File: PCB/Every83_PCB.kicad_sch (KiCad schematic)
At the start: 42 parts, among them J1 781710004, J2 Conn_01x08_Socket, J3 Conn_01x02_Socket, J4 Conn_01x03_Pin, J5 Conn_01x08_Socket, J6 Conn_01x02_Pin, J7 Conn_02x03_Counter_Clockwise, Q1 MMDT2222A, Q2 2N7002, Q3 DMG2305, Q4 AO3401A, SW101 KMR2, SW102 KMR2, U1 Core52840, U2 AP2112(3.3V), U3 MCP73831T-2ACI/OT

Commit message: Removing neopixels WIP
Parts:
- removed R16: 470R, Resistor_SMD:R_0603_1608Metric, symbol Device:R
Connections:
- net 3.3V: no longer Q4.3 (D), R15.2
- net V_Raw: now reaches C7.2, D101.1 (C), Q3.2 (S), R8.2, U2.1 (IN)
- net V_Raw: now also Q4.3 (D), R15.2
- no-connect marks 1 -> 2
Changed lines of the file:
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@@
 	)
 	(no_connect
+		(at 167.64 109.22)
+	)
+	(no_connect
 		(at 180.34 245.11)
 	)
@@
 		)
 	)
+	(global_label "V_Raw"
+		(shape input)
+		(at 149.86 240.03 90)
+		(fields_autoplaced yes)
+		(effects
+			(font
+				(size 1.27 1.27)
+			)
+			(justify left)
+		)
+		(property "Intersheetrefs" "${INTERSHEET_REFS}"
+			(at 149.86 231.2391 90)
+			(effects
+				(font
+					(size 1.27 1.27)
+				)
+				(justify left)
+				(hide yes)
+			)
+		)
+	)
 	(global_label "16"
 		(shape input)
@@
 		)
 	)
-	(global_label "NEOPIX"
+	(global_label "V_Raw"
 		(shape input)
-		(at 175.26 109.22 0)
+		(at 251.46 168.91 90)
 		(fields_autoplaced yes)
 		(effects
@@
 		)
 		(property "Intersheetrefs" "${INTERSHEET_REFS}"
-			(at 185.1395 109.22 0)
+			(at 251.46 160.1191 90)
 			(effects
 				(font
@@
 	)
 	(symbol
-		(lib_id "Device:R")
-		(at 171.45 109.22 270)
-		(unit 1)
-		(exclude_from_sim no)
-		(in_bom yes)
-		(on_board yes)
-		(dnp no)
-		(fields_autoplaced yes)
-		(property "Reference" "R16"
-			(at 171.45 102.87 90)
-			(effects
-				(font
-					(size 1.27 1.27)
-				)
-			)
-		)
-		(property "Value" "470R"
-			(at 171.45 105.41 90)
-			(effects
-				(font
-					(size 1.27 1.27)
-				)
-			)
-		)
-		(property "Footprint" "Resistor_SMD:R_0603_1608Metric"
-			(at 171.45 107.442 90)
-			(effects
-				(font
-					(size 1.27 1.27)
-				)
-				(hide yes)
-			)
-		)
-		(property "Datasheet" "~"
-			(at 171.45 109.22 0)
-			(effects
-				(font
-					(size 1.27 1.27)
-				)
-				(hide yes)
-			)
-		)
-		(property "Description" "Resistor"
-			(at 171.45 109.22 0)
-			(effects
-				(font
-					(size 1.27 1.27)
-				)
-				(hide yes)
-			)
-		)
-		(pin "1"
-		)
-		(pin "2"
-		)
-		(instances
-			(project "Every83_PCB"
-				(path "/ea2432c4-eb7a-431a-b465-8c00cfcb4450"
-					(reference "R16")
-					(unit 1)
-				)
-			)
-		)
-	)
-	(symbol
 		(lib_id "Adafruit nRF52840 Bluefruit Feather Express Rev D-eagle-import:SWITCH_TACT_SMT4.6X2.8")
 		(at 66.04 187.96 0)
@@
 					(unit 1)
 				)
-			)
-		)
-	)
-	(symbol
-		(lib_id "Adafruit nRF52840 Bluefruit Feather Express Rev D-eagle-import:3.3V")
-		(at 251.46 166.37 0)
-		(unit 1)
-		(exclude_from_sim no)
-		(in_bom yes)
-		(on_board yes)
-		(dnp no)
-		(property "Reference" "#U$039"
-			(at 251.46 166.37 0)
-			(effects
-				(font
-					(size 1.27 1.27)
-				)
-				(hide yes)
-			)
-		)
-		(property "Value" "3.3V"
-			(at 249.936 165.354 0)
-			(effects
-				(font
-					(size 1.27 1.0795)
-				)
-				(justify left bottom)
-			)
-		)
-		(property "Footprint" ""
-			(at 251.46 166.37 0)
-			(effects
-				(font
-					(size 1.27 1.27)
-				)
-				(hide yes)
-			)
-		)
-		(property "Datasheet" ""
-			(at 251.46 166.37 0)
-			(effects
-				(font
-					(size 1.27 1.27)
-				)
-				(hide yes)
-			)
-		)
-		(property "Description" ""
-			(at 251.46 166.37 0)
-			(effects
-				(font
-					(size 1.27 1.27)
-				)
-				(hide yes)
-			)
-		)
-		(pin "1"
-		)
-		(instances
-			(project "Every83_PCB"
-				(path "/ea2432c4-eb7a-431a-b465-8c00cfcb4450"
-					(reference "#U$039")
-					(unit 1)
-				)

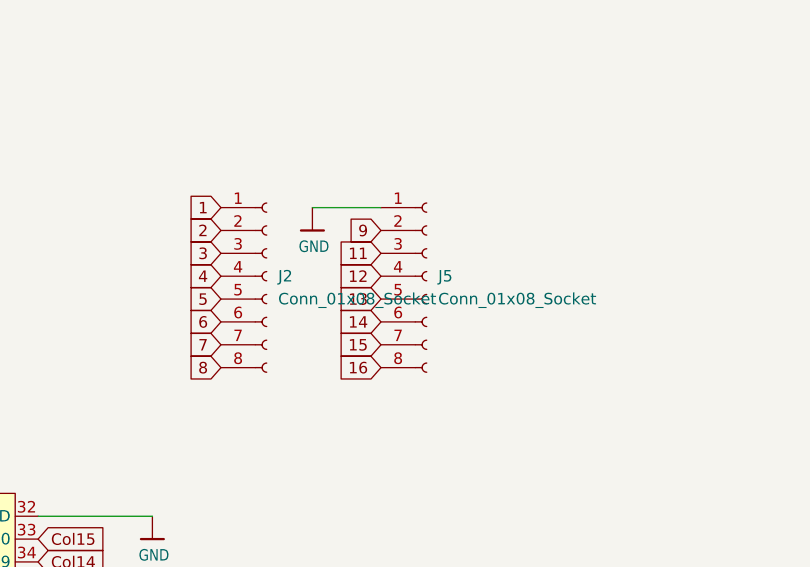
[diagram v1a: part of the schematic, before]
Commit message: removed pin headers
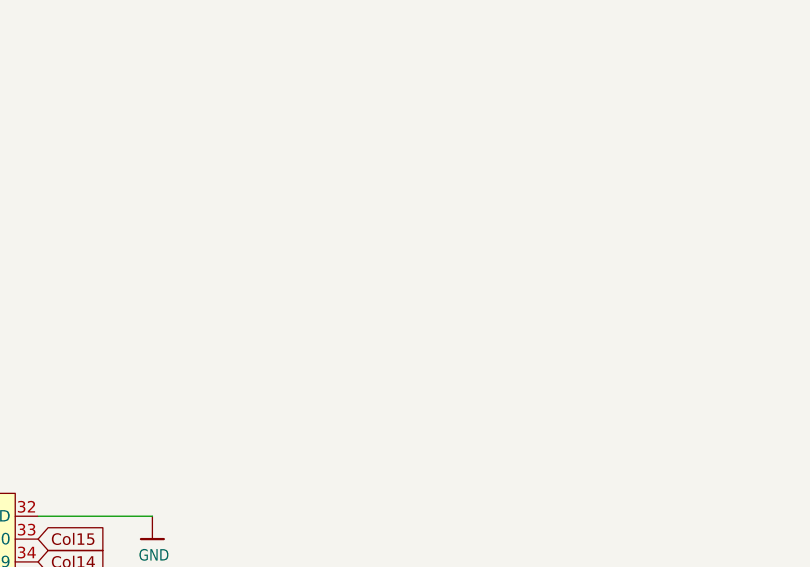
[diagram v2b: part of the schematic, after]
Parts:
- removed J2, J5: Conn_01x08_Socket, Connector_PinHeader_1.27mm:PinHeader_1x08_P1.27mm_Vertical, symbol Connector:Conn_01x08_Socket

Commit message: WIP
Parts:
- C3, C4: footprint Adafruit nRF52840 Bluefruit Feather Express Rev D:0603-NO -> Capacitor_SMD:C_0402_1005Metric
- C5, C7, C8: footprint Adafruit nRF52840 Bluefruit Feather Express Rev D:0805-NO -> Capacitor_SMD:C_0603_1608Metric
- C6, C9: value 10uF -> 4.7uF; footprint Adafruit nRF52840 Bluefruit Feather Express Rev D:0805-NO -> Capacitor_SMD:C_0603_1608Metric
- R1, R10, R13, R14, R15, R6, R7, R8, R9: footprint Resistor_SMD:R_0603_1608Metric -> Resistor_SMD:R_0402_1005Metric
- R4: footprint Adafruit nRF52840 Bluefruit Feather Express Rev D:0603-NO -> Resistor_SMD:R_0402_1005Metric
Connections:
- net GND: now also R4.1; no longer R4.2
- net at U3.5 (PROG): now also R4.2; no longer R4.1
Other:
- moved on the sheet: C6, R4

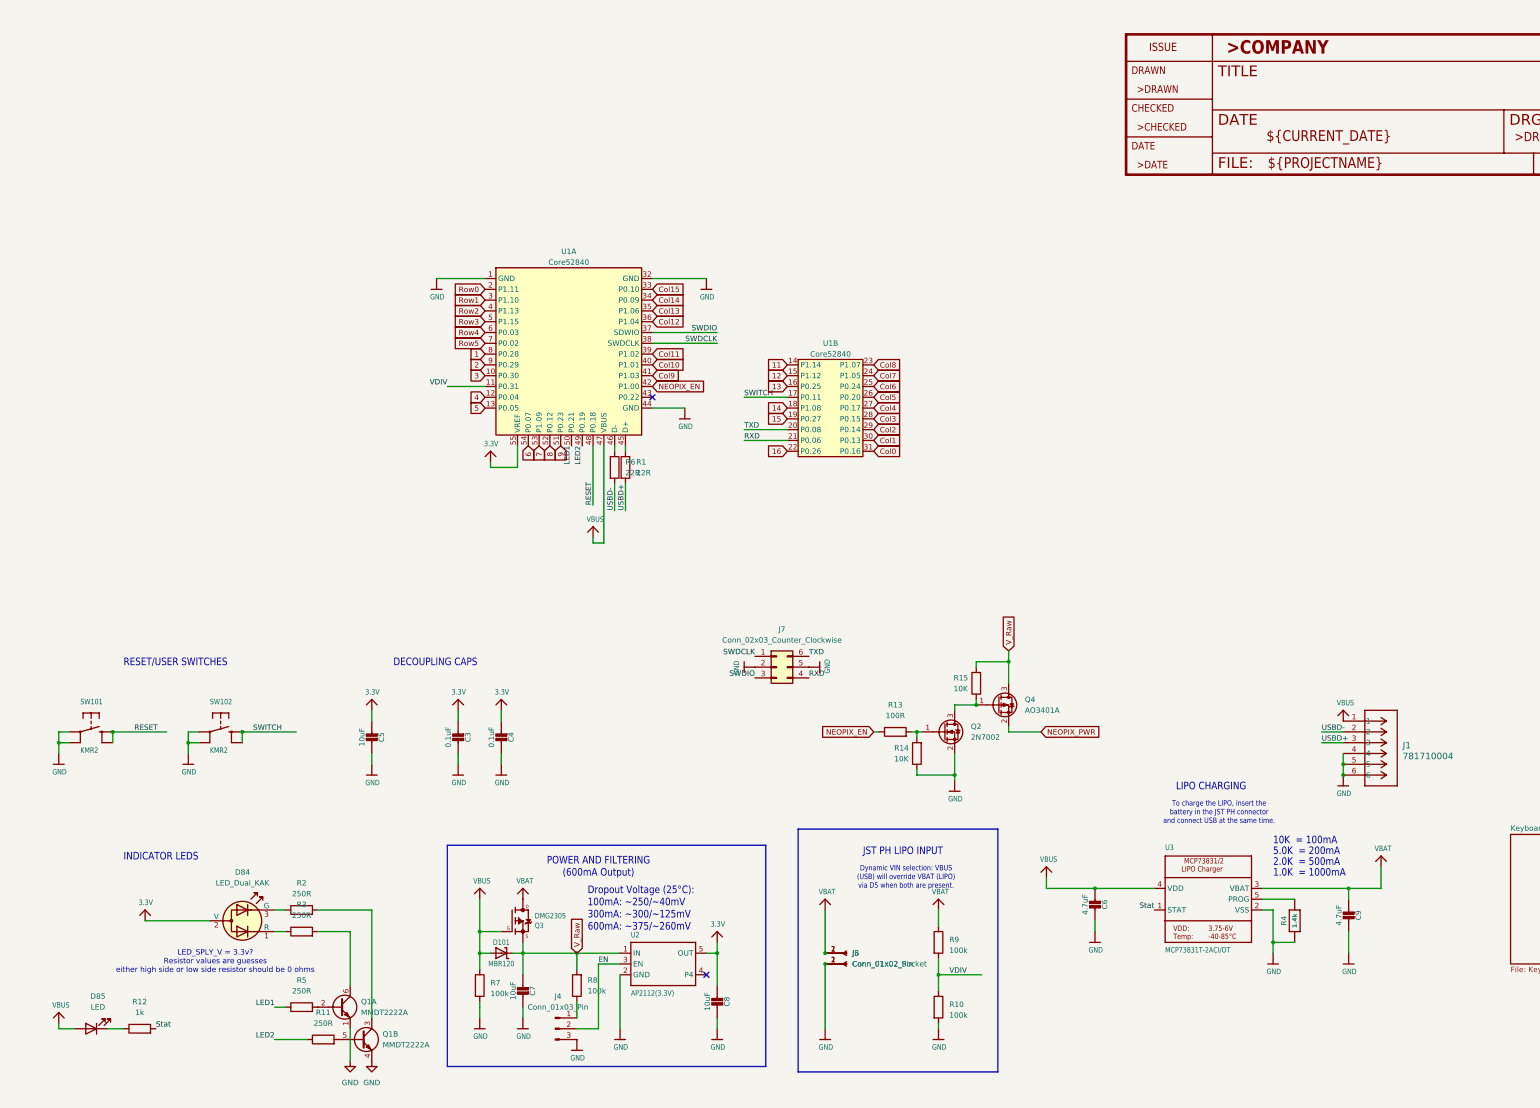
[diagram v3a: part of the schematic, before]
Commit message: Changed battery managment IC and LDO
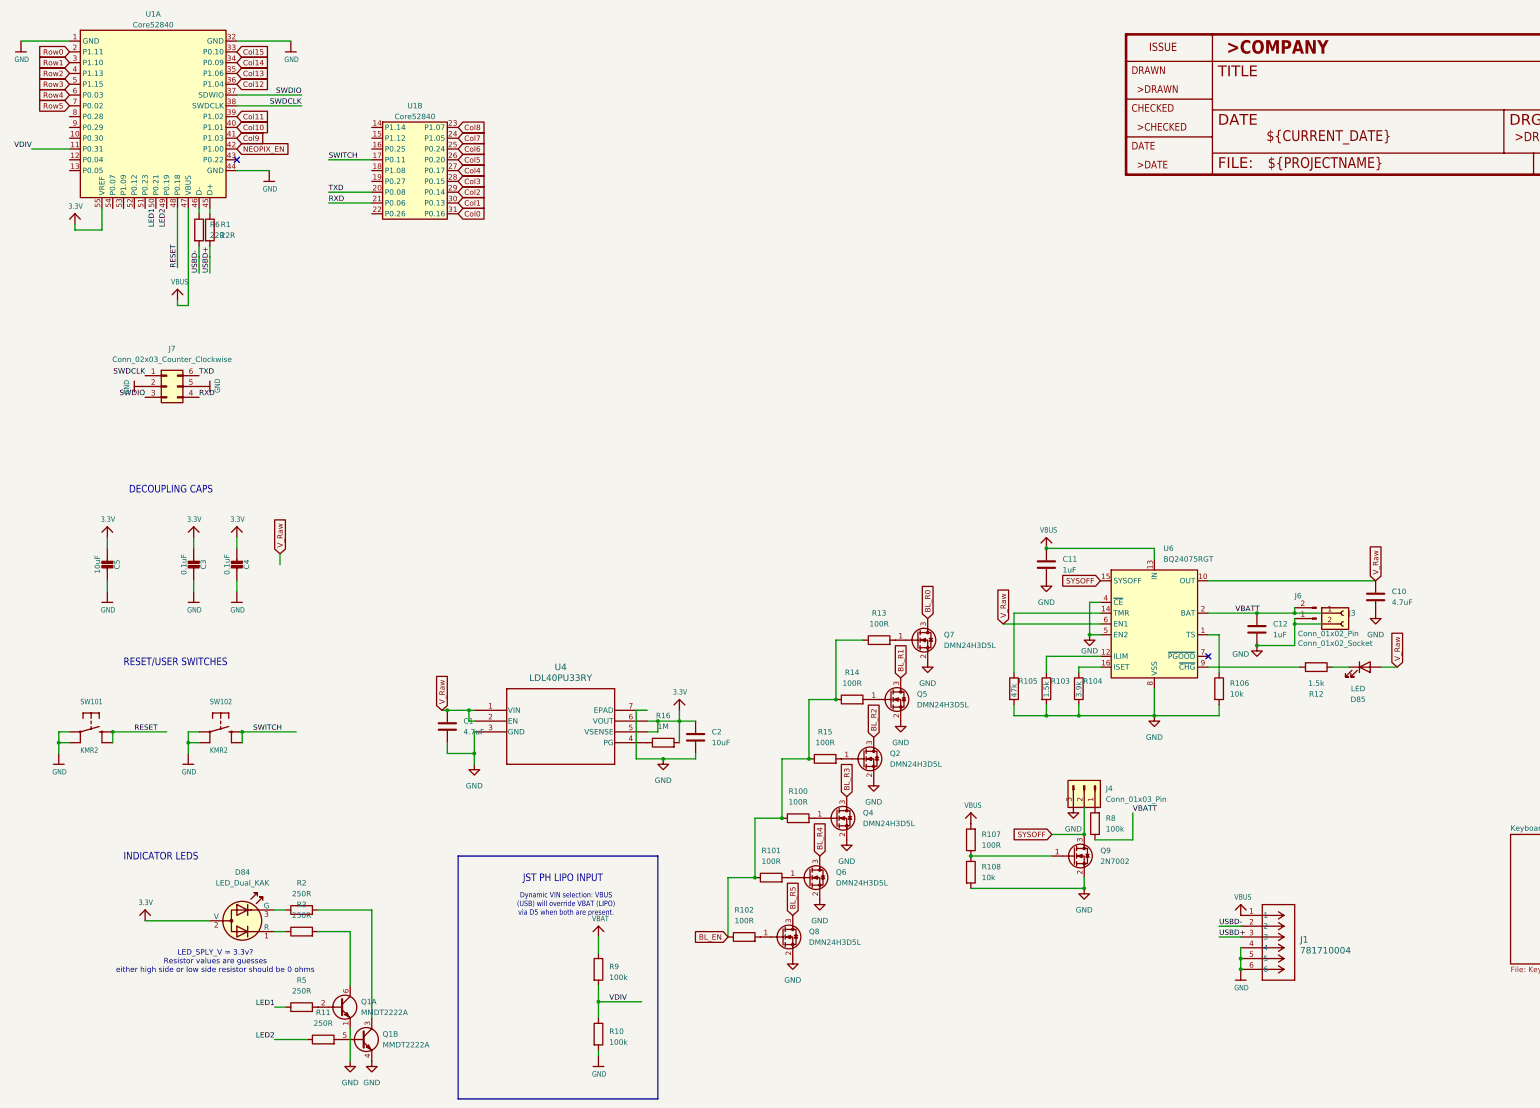
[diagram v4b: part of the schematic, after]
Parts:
- removed C6, C9: 4.7uF, Capacitor_SMD:C_0603_1608Metric, symbol Adafruit nRF52840 Bluefruit Feather Express Rev D-eagle-import:CAP_CERAMIC0805-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
- removed C7, C8: 10uF, Capacitor_SMD:C_0603_1608Metric, symbol Adafruit nRF52840 Bluefruit Feather Express Rev D-eagle-import:CAP_CERAMIC0805-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
- removed D101: MBR120, Diode_SMD:D_SOD-123, symbol Adafruit nRF52840 Bluefruit Feather Express Rev D-eagle-import:DIODE-SCHOTTKYSO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
- removed Q2: 2N7002, Package_TO_SOT_SMD:SOT-23, symbol Transistor_FET:2N7002
- removed Q3: DMG2305, Adafruit nRF52840 Bluefruit Feather Express Rev D:SOT23-R, symbol Adafruit nRF52840 Bluefruit Feather Express Rev D-eagle-import:MOSFET-P
- removed Q4: AO3401A, Package_TO_SOT_SMD:SOT-23, symbol Transistor_FET:AO3401A
- removed R4: 1.4k, Resistor_SMD:R_0402_1005Metric, symbol Adafruit nRF52840 Bluefruit Feather Express Rev D-eagle-import:RESISTOR_0603_NO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
- removed R7: 100k, Resistor_SMD:R_0402_1005Metric, symbol Device:R
- removed U2: AP2112(3.3V), Adafruit nRF52840 Bluefruit Feather Express Rev D:SOT23-5, symbol Adafruit nRF52840 Bluefruit Feather Express Rev D-eagle-import:VREG_SOT23-5
- removed U3: MCP73831T-2ACI/OT, Adafruit nRF52840 Bluefruit Feather Express Rev D:SOT23-5, symbol Adafruit nRF52840 Bluefruit Feather Express Rev D-eagle-import:MCP73831/2
- added C1, C10: 4.7uF, Capacitor_SMD:C_0402_1005Metric, symbol Device:C
- added C11, C12: 1uF, Capacitor_SMD:C_0402_1005Metric, symbol Device:C
- added C2: 10uF, Capacitor_SMD:C_0402_1005Metric, symbol Device:C
- added Q2, Q4, Q5, Q6, Q7, Q8: DMN24H3D5L, Package_TO_SOT_SMD:SOT-23, symbol Transistor_FET:DMN24H3D5L
- added Q9: 2N7002, Package_TO_SOT_SMD:SOT-23, symbol Transistor_FET:2N7002
- added R100, R101, R102, R107: 100R, Resistor_SMD:R_0402_1005Metric, symbol Device:R
- added R103: 1.5k, Resistor_SMD:R_0402_1005Metric, symbol Device:R
- added R104: 3.9k, Resistor_SMD:R_0402_1005Metric, symbol Device:R
- added R105: 47k, Resistor_SMD:R_0402_1005Metric, symbol Device:R
- added R106, R108: 10k, Resistor_SMD:R_0402_1005Metric, symbol Device:R
- added R16: 1M, Resistor_SMD:R_0402_1005Metric, symbol Device:R
- added U4: LDL40PU33RY, footprints:DFN6_2X2-0p65_WETTABLEFLANKS_STM-L, symbol LDL40:LDL40PU33RY
- added U6: BQ24075RGT, Package_DFN_QFN:VQFN-16-1EP_3x3mm_P0.5mm_EP1.6x1.6mm, symbol Battery_Management:BQ24075RGT
- C5: footprint Capacitor_SMD:C_0603_1608Metric -> Capacitor_SMD:C_0402_1005Metric
- R12: value 1k -> 1.5k
- R14, R15: value 10K -> 100R
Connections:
- net 3.3V: now also C2.1, R16.2, U4.5 (VSENSE), U4.6 (VOUT)
- net GND: now also C1.2, C10.2, C11.2, C12.2, C2.2, Q2.2 (S), Q4.2 (S), Q5.2 (S), Q6.2 (S), Q7.2 (S), Q8.2 (S), Q9.2 (S), R103.2, R104.2, R105.2, R106.2, R108.2, U4.3 (GND), U4.7 (EPAD), U6.17 (VSS), U6.4 (~{CE}), U6.5 (EN2), U6.8 (VSS); no longer R14.1
- net NEOPIX_EN: no longer R13.1
- net VBAT: no longer J3.1 (Pin_1), J6.2 (Pin_2)
- net VBUS: now also C11.1, R107.2, U6.13 (IN); no longer D85.2 (A)
- net V_Raw: now also D85.2 (A), C1.1, C10.1, U4.1 (VIN), U4.2 (EN), U6.10 (OUT), U6.11 (OUT), U6.6 (EN1); no longer R15.2, R8.2
- net at R14.2: now also Q5.1 (G); no longer R13.2
- net BL_EN: now reaches R15.1
- net BL_EN: now also R13.1, R14.1, R100.1, R101.1, R102.1
- net at J4.1 (Pin_1): now also R8.2; no longer R8.1
- net 1: no longer names the net of U1.8 (P0.28)
- net 11: no longer names the net of U1.14 (P1.14)
- net 12: no longer names the net of U1.15 (P1.12)
- net 13: no longer names the net of U1.16 (P0.25)
- net 14: no longer names the net of U1.18 (P1.08)
- net 15: no longer names the net of U1.19 (P0.27)
- net 16: no longer names the net of U1.22 (P0.26)
- net 2: no longer names the net of U1.9 (P0.29)
- net 3: no longer names the net of U1.10 (P0.30)
- net 4: no longer names the net of U1.12 (P0.04)
- net 5: no longer names the net of U1.13 (P0.05)
- net 6: no longer names the net of U1.54 (P0.07)
- net 7: no longer names the net of U1.53 (P1.09)
- net 8: no longer names the net of U1.52 (P0.12)
- net 9: no longer names the net of U1.51 (P0.23)
- net EN renamed SYSOFF
- net SYSOFF: now also Q9.3 (D), U6.15 (SYSOFF)
- net Stat: no longer names the net of R12.2
- net Stat: now also U6.9 (~{CHG})
- new net: Q6.1 (G), R101.2
- new net: Q4.1 (G), R100.2
- new net: R104.1, U6.16 (ISET)
- new net: Q9.1 (G), R107.1, R108.1
- new net: R105.1, U6.14 (TMR)
- new net: Q8.1 (G), R102.2
- new net: Q7.1 (G), R13.2
- new net: Q2.1 (G), R15.2
- new net: R16.1, U4.4 (PG)
- new net: R106.1, U6.1 (TS)
- new net: R103.1, U6.12 (ILIM)
- new net BL_R0: Q7.3 (D)
- new net BL_R1: Q5.3 (D)
- new net BL_R2: Q2.3 (D)
- new net BL_R3: Q4.3 (D)
- new net BL_R4: Q6.3 (D)
- new net BL_R5: Q8.3 (D)
- new net VBATT: C12.1, J3.1 (Pin_1), J6.2 (Pin_2), R8.1, U6.2 (BAT), U6.3 (BAT)
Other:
- note removed: "1.0K = 1000mA"
- note removed: "10K = 100mA"
- note removed: "2.0K = 500mA"
- note removed: "5.0K = 200mA"
- note removed: "Dropout Voltage (25°C): 100mA: ~250/~40mV 300mA: ~300/~125mV 600mA: ~375/~260mV"
- note removed: "LIPO CHARGING"
- note removed: "POWER AND FILTERING (600mA Output)"
- note removed: "To charge the LIPO, insert the battery in the JST PH connector and connect USB at the same time."
- moved on the sheet: C3, C4, C5, D85, J1, J6, J7, R1, R10, R12, R6, R8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

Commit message: Orginizing and small work done
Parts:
- removed C10: 4.7uF, Capacitor_SMD:C_0402_1005Metric, symbol Device:C
- removed C11, C12: 1uF, Capacitor_SMD:C_0402_1005Metric, symbol Device:C
- removed D85: LED, JohnDeereLibrary:LED_WURTH_155060AS75300, symbol Device:LED
- removed J3: Conn_01x02_Socket, Connector_PinHeader_2.54mm:PinHeader_1x02_P2.54mm_Vertical, symbol Connector:Conn_01x02_Socket
- removed J4: Conn_01x03_Pin, Connector_Molex:Molex_Pico-EZmate_78171-0003_1x03-1MP_P1.20mm_Vertical, symbol Connector:Conn_01x03_Pin
- removed J6: Conn_01x02_Pin, Connector_Molex:Molex_Pico-EZmate_78171-0002_1x02-1MP_P1.20mm_Vertical, symbol Connector:Conn_01x02_Pin
- removed Q9: 2N7002, Package_TO_SOT_SMD:SOT-23, symbol Transistor_FET:2N7002
- removed R103, R12: 1.5k, Resistor_SMD:R_0402_1005Metric, symbol Device:R
- removed R104: 3.9k, Resistor_SMD:R_0402_1005Metric, symbol Device:R
- removed R105: 47k, Resistor_SMD:R_0402_1005Metric, symbol Device:R
- removed R106, R108: 10k, Resistor_SMD:R_0402_1005Metric, symbol Device:R
- removed R107: 100R, Resistor_SMD:R_0402_1005Metric, symbol Device:R
- removed R8: 100k, Resistor_SMD:R_0402_1005Metric, symbol Device:R
- removed U6: BQ24075RGT, Package_DFN_QFN:VQFN-16-1EP_3x3mm_P0.5mm_EP1.6x1.6mm, symbol Battery_Management:BQ24075RGT
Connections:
- no-connect marks 2 -> 1
